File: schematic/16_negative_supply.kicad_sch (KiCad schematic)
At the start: 20 parts, among them U702 LT1054CP, U706 L7905CV

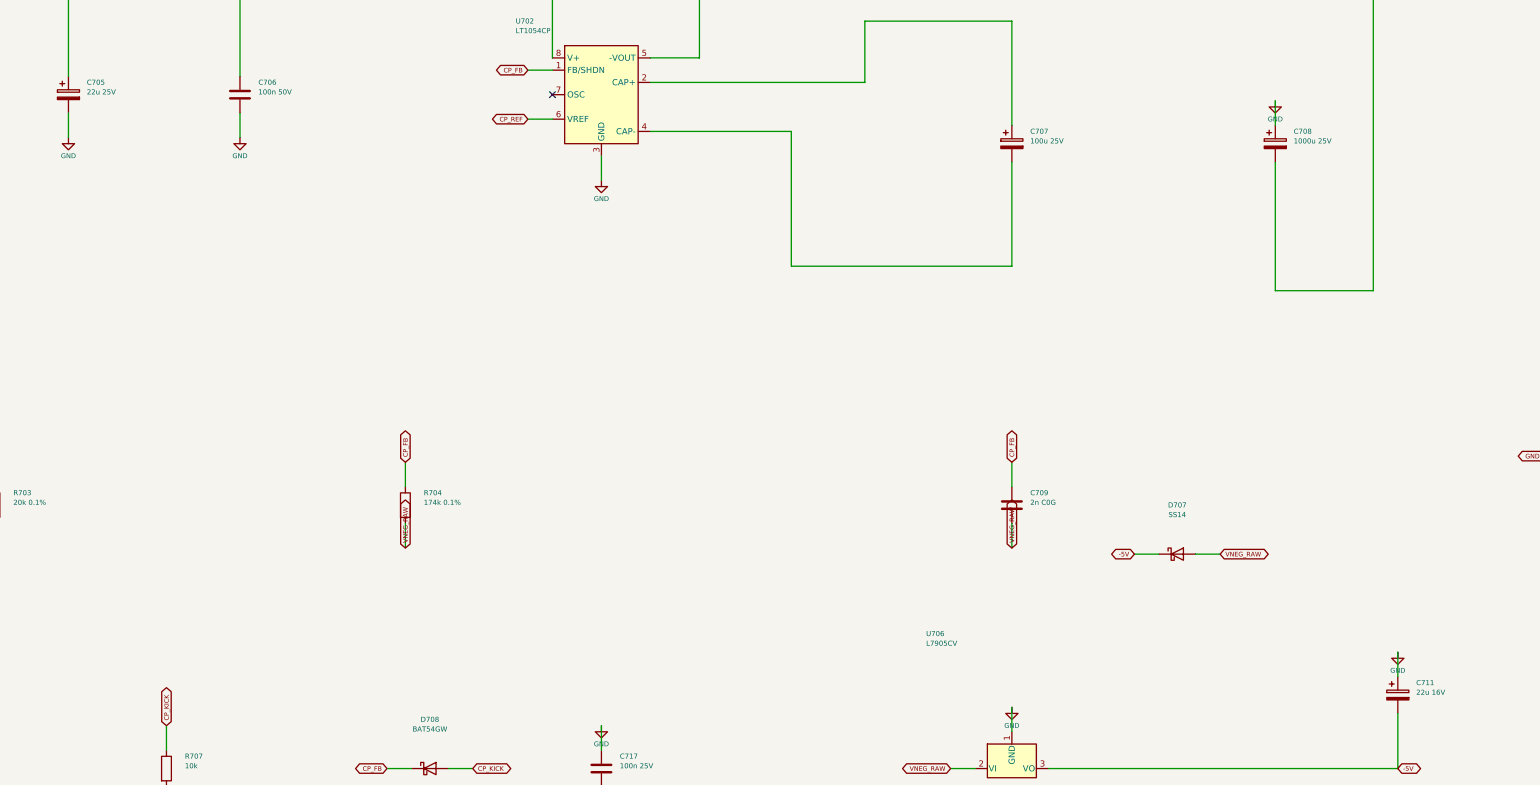
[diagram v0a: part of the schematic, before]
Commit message: pick controls and start pcb placement
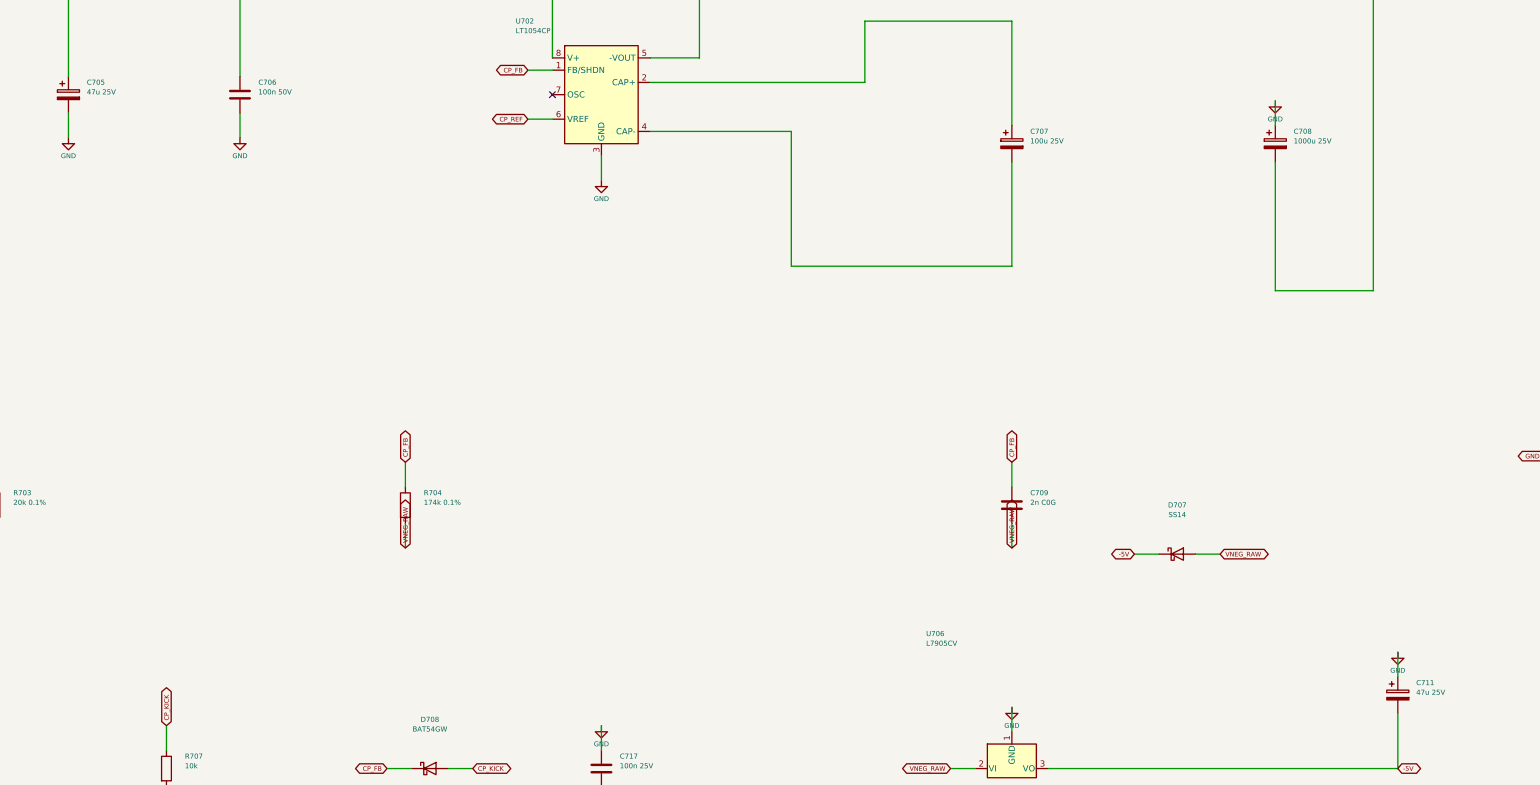
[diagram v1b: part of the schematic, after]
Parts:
- C705: value 22u 25V -> 47u 25V; MPN (none) -> 25YXJ47M5X11; Manufacturer (none) -> Rubycon; Supplier (none) -> DigiKey; Supplier URL (none) -> https://www.digikey.com/en/products/detail/rubycon/25YXJ47M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
- C708: MPN (none) -> EEU-FR1E102; Manufacturer (none) -> Panasonic; Supplier (none) -> Mouser; Supplier URL (none) -> https://www.mouser.com/en/ProductDetail/Panasonic-Industry/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
- C711: value 22u 16V -> 47u 25V; MPN (none) -> 25YXJ47M5X11; Manufacturer (none) -> Rubycon; Supplier (none) -> DigiKey; Supplier URL (none) -> https://www.digikey.com/en/products/detail/rubycon/25YXJ47M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
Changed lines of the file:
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@@
       )
     )
-    (property "Value" "22u 25V"
+    (property "Value" "47u 25V"
       (at 78.74000000000001 99.78999999999999 0.0)
       (effects
@@
         )
         (justify left)
+        (hide yes)
+      )
+    )
+    (property "MPN" "25YXJ47M5X11"
+      (at 74.93 100.33 0.0)
+      (effects
+        (font
+          (size 1.0 1.0)
+        )
+        (hide yes)
+      )
+    )
+    (property "Manufacturer" "Rubycon"
+      (at 74.93 100.33 0.0)
+      (effects
+        (font
+          (size 1.0 1.0)
+        )
+        (hide yes)
+      )
+    )
+    (property "Supplier" "DigiKey"
+      (at 74.93 100.33 0.0)
+      (effects
+        (font
+          (size 1.0 1.0)
+        )
+        (hide yes)
+      )
+    )
+    (property "Supplier URL" "https://www.digikey.com/en/products/detail/rubycon/25YXJ47M5X11/3562900"
+      (at 74.93 100.33 0.0)
+      (effects
+        (font
+          (size 1.0 1.0)
+        )
         (hide yes)
       )
@@
       )
     )
+    (property "MPN" "EEU-FR1E102"
+      (at 325.12 110.49 0.0)
+      (effects
+        (font
+          (size 1.0 1.0)
+        )
+        (hide yes)
+      )
+    )
+    (property "Manufacturer" "Panasonic"
+      (at 325.12 110.49 0.0)
+      (effects
+        (font
+          (size 1.0 1.0)
+        )
+        (hide yes)
+      )
+    )
+    (property "Supplier" "Mouser"
+      (at 325.12 110.49 0.0)
+      (effects
+        (font
+          (size 1.0 1.0)
+        )
+        (hide yes)
+      )
+    )
+    (property "Supplier URL" "https://www.mouser.com/en/ProductDetail/Panasonic-Industry/EEU-FR1E102?qs=Ao3mORb5HCARq2G4MnAlEQ%3D%3D"
+      (at 325.12 110.49 0.0)
+      (effects
+        (font
+          (size 1.0 1.0)
+        )
+        (hide yes)
+      )
+    )
     (instances
       (project "arpeggiator"
@@
       )
     )
-    (property "Value" "22u 16V"
+    (property "Value" "47u 25V"
       (at 354.33 224.25 0.0)
       (effects
@@
         (hide yes)
       )
+    )
+    (property "MPN" "25YXJ47M5X11"
+      (at 350.52 224.79 0.0)
+      (effects
+        (font
+          (size 1.0 1.0)
+        )
+        (hide yes)
+      )
+    )
+    (property "Manufacturer" "Rubycon"
+      (at 350.52 224.79 0.0)
+      (effects
+        (font
+          (size 1.0 1.0)
+        )
+        (hide yes)
+      )
+    )
+    (property "Supplier" "DigiKey"
+      (at 350.52 224.79 0.0)
+      (effects
+        (font
+          (size 1.0 1.0)
+        )
+        (hide yes)
+      )
+    )
+    (property "Supplier URL" "https://www.digikey.com/en/products/detail/rubycon/25YXJ47M5X11/3562900"
+      (at 350.52 224.79 0.0)
+      (effects
+        (font
+          (size 1.0 1.0)
+        )
+        (hide yes)
+      )

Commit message: parts and cheaper PCB files
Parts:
- C707: MPN EEU-FR1E101 -> EEU-FC1E101S; Supplier URL https://www.mouser.com/en/ProductDetail/Panasonic-Industry/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 -> https://www.mouser.com/en/ProductDetail/Panasonic/EEU-FC1E1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
- D704, D707: MPN SS14-13-F -> SS14-E3/61T; Manufacturer Diodes Incorporated -> Vishay; Supplier LCSC -> Mouser
- D708: MPN BAT54GW,115 -> BAT54GWX
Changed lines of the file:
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@@
       )
     )
-    (property "Datasheet" ""
+    (property "Datasheet" "https://industrial.panasonic.com/cdbs/www-data/pdf/RDF0000/ABA0000C1209.pdf"
       (at 274.32 107.94999999999999 0.0)
       (effects
@@
       )
     )
-    (property "MPN" "EEU-FR1E101"
+    (property "MPN" "EEU-FC1E101S"
       (at 270.51 110.49 0.0)
       (effects
@@
       )
     )
-    (property "Supplier URL" "https://www.mouser.com/en/ProductDetail/Panasonic-Industry/EEU-FR1E101?qs=Ao3mORb5HCDieoJwtkb8Dw%3D%3D"
+    (property "Supplier URL" "https://www.mouser.com/en/ProductDetail/Panasonic/EEU-FC1E101S?qs=XZT10BZ%2FaGG7SbPLggsp3w%3D%3D"
       (at 270.51 110.49 0.0)
       (effects
@@
       )
     )
-    (property "Datasheet" "https://www.diodes.com/assets/Datasheets/ds23001.pdf"
+    (property "Datasheet" "https://www.mouser.com/datasheet/2/427/VISH_S_A0010526100_1-2571162.pdf"
       (at 304.8 185.42000000000002 0.0)
       (effects
@@
       )
     )
-    (property "MPN" "SS14-13-F"
+    (property "MPN" "SS14-E3/61T"
       (at 304.8 195.58 0.0)
       (effects
@@
       )
     )
-    (property "Manufacturer" "Diodes Incorporated"
+    (property "Manufacturer" "Vishay"
       (at 304.8 195.58 0.0)
       (effects
@@
       )
     )
-    (property "Supplier" "LCSC"
+    (property "Supplier" "Mouser"
       (at 304.8 195.58 0.0)
       (effects
@@
       )
     )
-    (property "Datasheet" "https://www.diodes.com/assets/Datasheets/ds23001.pdf"
+    (property "Datasheet" "https://www.mouser.com/datasheet/2/427/VISH_S_A0010526100_1-2571162.pdf"
       (at 389.89 165.1 0.0)
       (effects
@@
       )
     )
-    (property "MPN" "SS14-13-F"
+    (property "MPN" "SS14-E3/61T"
       (at 389.89 175.26 0.0)
       (effects
@@
       )
     )
-    (property "Manufacturer" "Diodes Incorporated"
+    (property "Manufacturer" "Vishay"
       (at 389.89 175.26 0.0)
       (effects
@@
       )
     )
-    (property "Supplier" "LCSC"
+    (property "Supplier" "Mouser"
       (at 389.89 175.26 0.0)
       (effects
@@
       )
     )
-    (property "MPN" "BAT54GW,115"
+    (property "MPN" "BAT54GWX"
       (at 149.86 240.03 0.0)
       (effects
